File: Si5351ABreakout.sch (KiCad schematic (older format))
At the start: 15 parts, among them J1 Power/Data, J2 SMA-F, J3 SMA-F, J4 SMA-F, J5 CLK0, J6 CLK1, J7 CLK2, T1 TC1-6X+, T2 TC1-6X+, T3 TC1-6X+, U1 SI5351A, X1 ECS-250-8-30B-CKM

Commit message: Schematic fix
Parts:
- T1, T2, T3: value TC1-6X+ -> Mini-Circuits TC1-6X+
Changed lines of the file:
@@
 Sheet 1 1
 Title "Si5351A Breakout"
-Date "30 May 2014"
+Date "07 Jul 2014"
 Rev "A"
 Comp "Etherkit"
@@
 U 1 1 538907B7
 P 7495 2330
-F 0 "T1" H 7435 2365 50  0000 C CNN
-F 1 "TC1-6X+" H 7305 2285 50  0000 C CNN
+F 0 "T1" H 6965 2055 50  0000 C CNN
+F 1 "Mini-Circuits TC1-6X+" H 7370 1975 50  0000 C CNN
 F 2 "" H 7495 2330 60  0000 C CNN
 F 3 "" H 7495 2330 60  0000 C CNN
@@
 U 1 1 538908A7
 P 7495 3080
-F 0 "T2" H 7435 3115 50  0000 C CNN
-F 1 "TC1-6X+" H 7305 3035 50  0000 C CNN
+F 0 "T2" H 7075 2800 50  0000 C CNN
+F 1 "Mini-Circuits TC1-6X+" H 7475 2715 50  0000 C CNN
 F 2 "" H 7495 3080 60  0000 C CNN
 F 3 "" H 7495 3080 60  0000 C CNN
@@
 U 1 1 53890928
 P 7480 3900
-F 0 "T3" H 7420 3935 50  0000 C CNN
-F 1 "TC1-6X+" H 7290 3855 50  0000 C CNN
+F 0 "T3" H 7050 3620 50  0000 C CNN
+F 1 "Mini-Circuits TC1-6X+" H 7445 3535 50  0000 C CNN
 F 2 "" H 7480 3900 60  0000 C CNN
 F 3 "" H 7480 3900 60  0000 C CNN

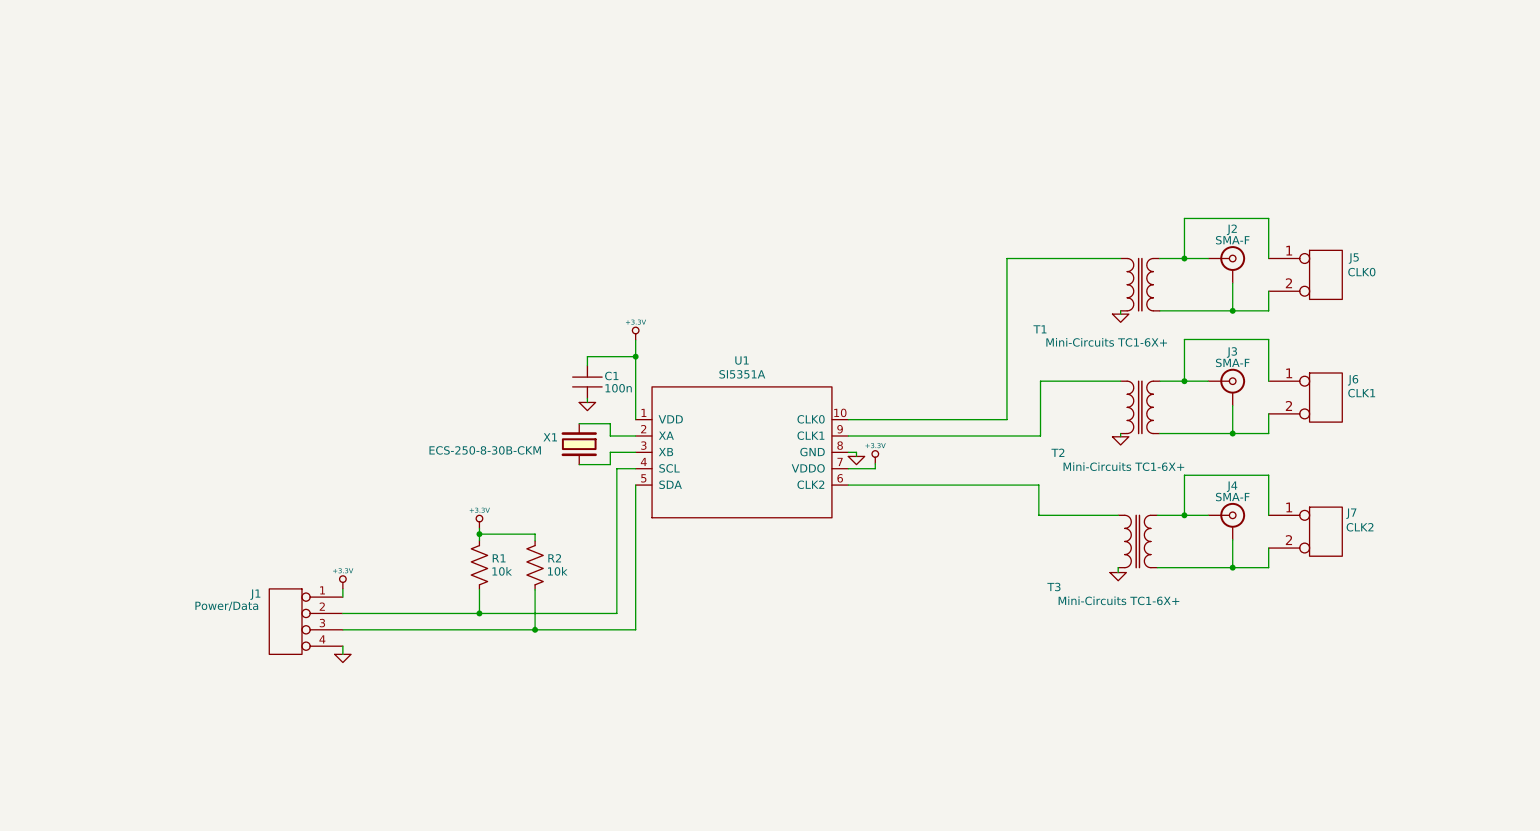
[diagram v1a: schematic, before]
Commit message: Rev B - I2C level conv, voltage regulator
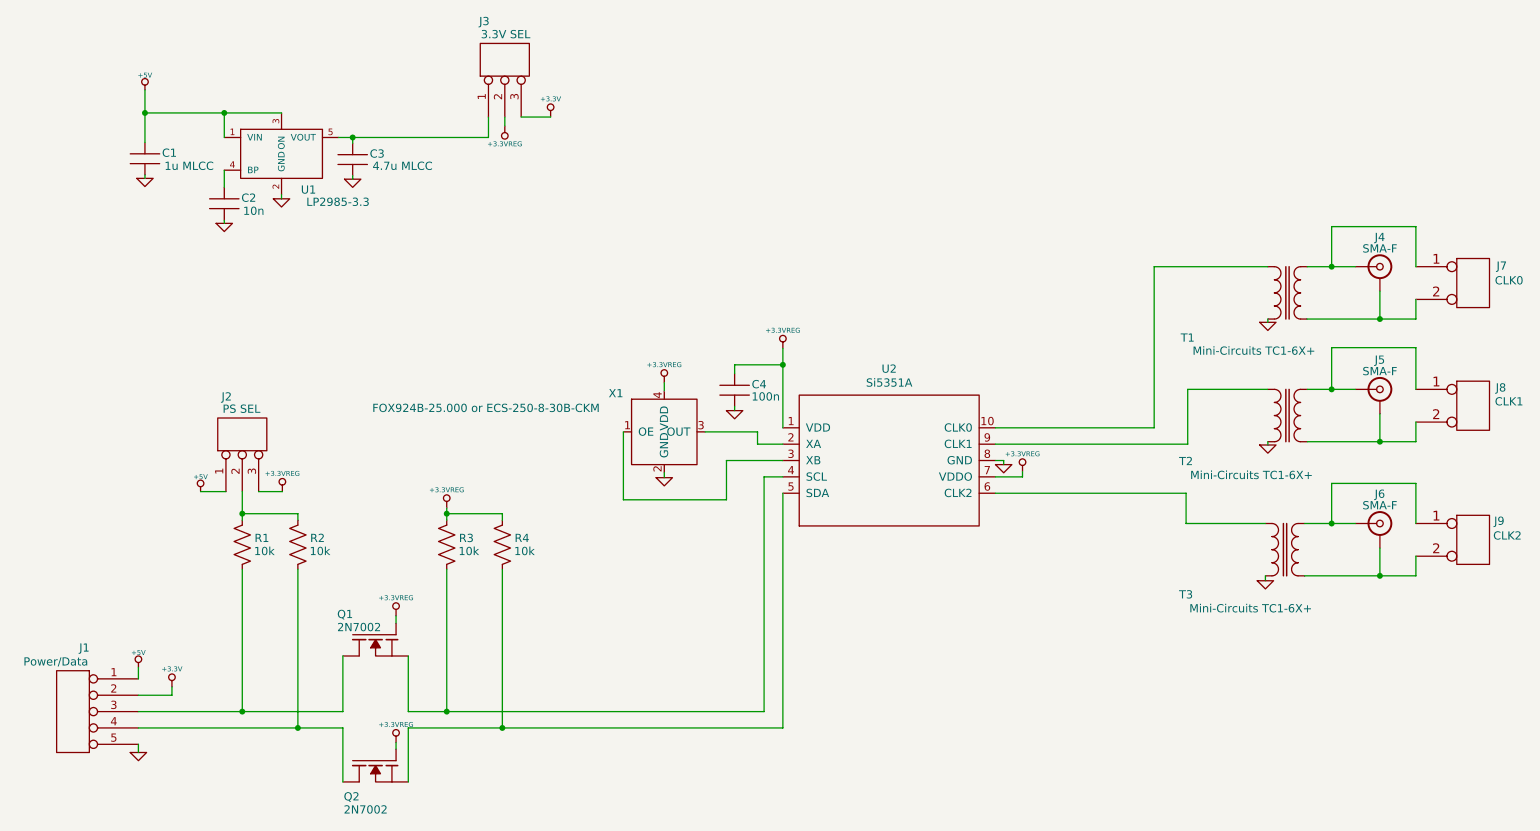
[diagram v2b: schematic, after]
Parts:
- removed J1: Power/Data, symbol CONN_4
- removed X1: ECS-250-8-30B-CKM, symbol CRYSTAL-SMD
- added C1: 1u MLCC, symbol C
- added C2: 10n, symbol C
- added C3: 4.7u MLCC, symbol C
- added J1: Power/Data, symbol CONN_5
- added J2: PS SEL, symbol CONN_3
- added J3: 3.3V SEL, symbol CONN_3
- added Q1, Q2: 2N7002, symbol MOSFET_N
- added R1, R2: 10k, symbol R
- added U1: LP2985-3.3, symbol LP2985
- added X1: FOX924B-25.000 or ECS-250-8-30B-CKM, symbol OSCILLATOR
- U2: renamed from U1; value SI5351A -> Si5351A
- renumbered C1 to C4, J2 to J4, J3 to J5, J4 to J6, J5 to J7, J6 to J8, J7 to J9, R1 to R3, R2 to R4
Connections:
- net +3.3V: now also J1.2, J3.3 (P3); no longer C4.1, R3.1, R4.1, U2.1 (VDD), U2.7 (VDDO)
- net GND: now also C1.2, C2.2, C3.2, J1.5, U1.2 (GND), X1.2 (GND)
- net at U2.2 (XA): now also X1.3 (OUT)
- net at U2.3 (XB): now also X1.1 (OE)
- net at R3.2, U2.4 (SCL): now also Q1.1 (S)
- net at R4.2, U2.5 (SDA): now also Q2.1 (S)
- new net: J1.3, Q1.3 (D), R1.2
- new net: J1.4, Q2.3 (D), R2.2
- new net: J2.2 (PM), R1.1, R2.1
- new net: C2.1, U1.4 (BP)
- new net: C3.1, J3.1 (P1), U1.5 (VOUT)
- new net +3.3VREG: C4.1, J2.3 (P3), J3.2 (PM), Q1.2 (G), Q2.2 (G), R3.1, R4.1, U2.1 (VDD), U2.7 (VDDO), X1.4 (VDD)
- new net +5V: C1.1, J1.1, J2.1 (P1), U1.1 (VIN), U1.3 (ON)
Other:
- moved on the sheet: C4, J4, J5, J6, J7, J8, J9, R3, R4, T1, T2, T3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

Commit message: Rev C updates
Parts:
- removed T1, T2, T3: Mini-Circuits TC1-6X+, symbol TC1-6X+
- added J10: Osc Power, symbol JUMPER
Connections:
- net +3.3VREG: now also J10.1; no longer X1.4 (VDD)
- net GND: now also J4.2 (Ext), J5.2 (Ext), J6.2 (Ext), J7.2 (PM), J8.2 (PM), J9.2 (PM)
- net at U2.10 (CLK0): now also J4.1 (In), J7.1 (P1)
- net at U2.6 (CLK2): now also J6.1 (In), J9.1 (P1)
- net at U2.9 (CLK1): now also J5.1 (In), J8.1 (P1)
- new net: J10.2, X1.4 (VDD)
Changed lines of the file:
@@
 LIBS:valves
 LIBS:Si5351ABreakout-cache
-EELAYER 24 0
+EELAYER 25 0
 EELAYER END
 $Descr USLetter 11000 8500
@@
 Sheet 1 1
 Title "Si5351A Breakout"
-Date "27 Jul 2014"
-Rev "B"
+Date "15 Jan 2015"
+Rev "C"
 Comp "Etherkit"
 Comment1 ""
@@
 L GND #PWR02
 U 1 1 538772F6
-P 8340 4140
-F 0 "#PWR02" H 8340 4140 30  0001 C CNN
-F 1 "GND" H 8340 4070 30  0001 C CNN
-F 2 "" H 8340 4140 60  0000 C CNN
-F 3 "" H 8340 4140 60  0000 C CNN
-	1    8340 4140
+P 9040 4160
+F 0 "#PWR02" H 9040 4160 30  0001 C CNN
+F 1 "GND" H 9040 4090 30  0001 C CNN
+F 2 "" H 9040 4160 60  0000 C CNN
+F 3 "" H 9040 4160 60  0000 C CNN
+	1    9040 4160
 	1    0    0    -1
 $EndComp
@@
 L GND #PWR03
 U 1 1 53877301
-P 8355 3310
-F 0 "#PWR03" H 8355 3310 30  0001 C CNN
-F 1 "GND" H 8355 3240 30  0001 C CNN
-F 2 "" H 8355 3310 60  0000 C CNN
-F 3 "" H 8355 3310 60  0000 C CNN
-	1    8355 3310
+P 9040 3340
+F 0 "#PWR03" H 9040 3340 30  0001 C CNN
+F 1 "GND" H 9040 3270 30  0001 C CNN
+F 2 "" H 9040 3340 60  0000 C CNN
+F 3 "" H 9040 3340 60  0000 C CNN
+	1    9040 3340
 	1    0    0    -1
 $EndComp
@@
 L GND #PWR04
 U 1 1 5387730C
-P 8355 2560
-F 0 "#PWR04" H 8355 2560 30  0001 C CNN
-F 1 "GND" H 8355 2490 30  0001 C CNN
-F 2 "" H 8355 2560 60  0000 C CNN
-F 3 "" H 8355 2560 60  0000 C CNN
-	1    8355 2560
+P 9040 2595
+F 0 "#PWR04" H 9040 2595 30  0001 C CNN
+F 1 "GND" H 9040 2525 30  0001 C CNN
+F 2 "" H 9040 2595 60  0000 C CNN
+F 3 "" H 9040 2595 60  0000 C CNN
+	1    9040 2595
 	1    0    0    -1
 $EndComp
@@
 F 3 "" H 5095 3100 60  0000 C CNN
 	1    5095 3100
-	1    0    0    -1
-$EndComp
-$Comp
-L TC1-6X+ T1
-U 1 1 538907B7
-P 8395 2380
-F 0 "T1" H 7865 2105 50  0000 C CNN
-F 1 "Mini-Circuits TC1-6X+" H 8270 2025 50  0000 C CNN
-F 2 "" H 8395 2380 60  0000 C CNN
-F 3 "" H 8395 2380 60  0000 C CNN
-	1    8395 2380
-	1    0    0    -1
-$EndComp
-$Comp
-L TC1-6X+ T2
-U 1 1 538908A7
-P 8395 3130
-F 0 "T2" H 7855 2850 50  0000 C CNN
-F 1 "Mini-Circuits TC1-6X+" H 8255 2765 50  0000 C CNN
-F 2 "" H 8395 3130 60  0000 C CNN
-F 3 "" H 8395 3130 60  0000 C CNN
-	1    8395 3130
-	1    0    0    -1
-$EndComp
-$Comp
-L TC1-6X+ T3
-U 1 1 53890928
-P 8380 3950
-F 0 "T3" H 7855 3675 50  0000 C CNN
-F 1 "Mini-Circuits TC1-6X+" H 8250 3590 50  0000 C CNN
-F 2 "" H 8380 3950 60  0000 C CNN
-F 3 "" H 8380 3950 60  0000 C CNN
-	1    8380 3950
 	1    0    0    -1
 $EndComp
@@
 	6740 3405 6740 3430
 Wire Wire Line
-	8580 3790 8890 3790
-Wire Wire Line
-	8595 2970 8890 2970
-Wire Wire Line
-	8595 2220 8890 2220
-Wire Wire Line
 	9260 2220 9260 1975
 Wire Wire Line
@@
 Connection ~ 8745 3790
 Wire Wire Line
-	8580 4110 9260 4110
-Wire Wire Line
 	9260 4110 9260 3990
 Wire Wire Line
-	8595 2540 9260 2540
-Wire Wire Line
 	9260 2540 9260 2420
 Wire Wire Line
-	8595 3290 9260 3290
-Wire Wire Line
 	9260 3290 9260 3170
 Wire Wire Line
-	9040 3120 9040 3290
+	9040 3120 9040 3340
 Connection ~ 9040 3290
 Wire Wire Line
-	9040 3940 9040 4110
+	9040 3940 9040 4160
 Connection ~ 9040 4110
 Wire Wire Line
-	9040 2370 9040 2540
+	9040 2370 9040 2595
 Connection ~ 9040 2540
 Wire Wire Line
@@
 Connection ~ 3335 3730
 Wire Wire Line
-	8355 2540 8355 2560
-Wire Wire Line
-	8355 3290 8355 3310
-Wire Wire Line
-	8340 4110 8340 4140
-Wire Wire Line
 	6690 3605 7855 3605
 Wire Wire Line
 	7855 3605 7855 3790
 Wire Wire Line
-	7855 3790 8340 3790
+	7855 3790 8890 3790
 Wire Wire Line
 	6690 3305 7865 3305
@@
 	7865 3305 7865 2970
 Wire Wire Line
-	7865 2970 8355 2970
+	7865 2970 8890 2970
 Wire Wire Line
 	6690 3205 7660 3205
@@
 	7660 3205 7660 2220
 Wire Wire Line
-	7660 2220 8355 2220
+	7660 2220 8890 2220
 Wire Wire Line
 	1655 4790 1655 4840
@@
 	4665 3480 4665 3510
 Wire Wire Line
-	4665 2930 4665 2980
+	4665 2520 4665 2570
 Wire Wire Line
 	4415 3230 4415 3645
@@
 L +3.3VREG #PWR019
 U 1 1 53D57D6D
-P 4665 2930
-F 0 "#PWR019" H 4665 2890 30  0001 C CNN
-F 1 "+3.3VREG" H 4665 3040 30  0000 C CNN
-F 2 "" H 4665 2930 60  0000 C CNN
-F 3 "" H 4665 2930 60  0000 C CNN
-	1    4665 2930
+P 4665 2520
+F 0 "#PWR019" H 4665 2480 30  0001 C CNN
+F 1 "+3.3VREG" H 4665 2630 30  0000 C CNN
+F 2 "" H 4665 2520 60  0000 C CNN
+F 3 "" H 4665 2520 60  0000 C CNN
+	1    4665 2520
 	1    0    0    -1
 $EndComp
@@
 	1    0    0    -1
 $EndComp
+Wire Wire Line
+	9260 4110 9040 4110
+Wire Wire Line
+	9260 3290 9040 3290
+Wire Wire Line
+	9260 2540 9040 2540
+$Comp
+L JUMPER J10
+U 1 1 54B82569
+P 4665 2745
+F 0 "J10" V 4630 2640 50  0000 C CNN
+F 1 "Osc Power" V 4705 2505 50  0000 C CNN
+F 2 "" H 4665 2745 60  0000 C CNN
+F 3 "" H 4665 2745 60  0000 C CNN
+	1    4665 2745
+	0    1    1    0
+$EndComp
+Wire Wire Line
+	4665 2920 4665 2980
 $EndSCHEMATC
